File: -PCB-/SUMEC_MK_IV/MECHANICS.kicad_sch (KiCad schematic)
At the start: 20 parts, among them J13 Conn_01x06_Socket, J14 Conn_01x06_Socket, SW2 SW_Push, SW3 SW_Push, SW4 SW_Push, SW5 SW_Push, SW6 SW_Push

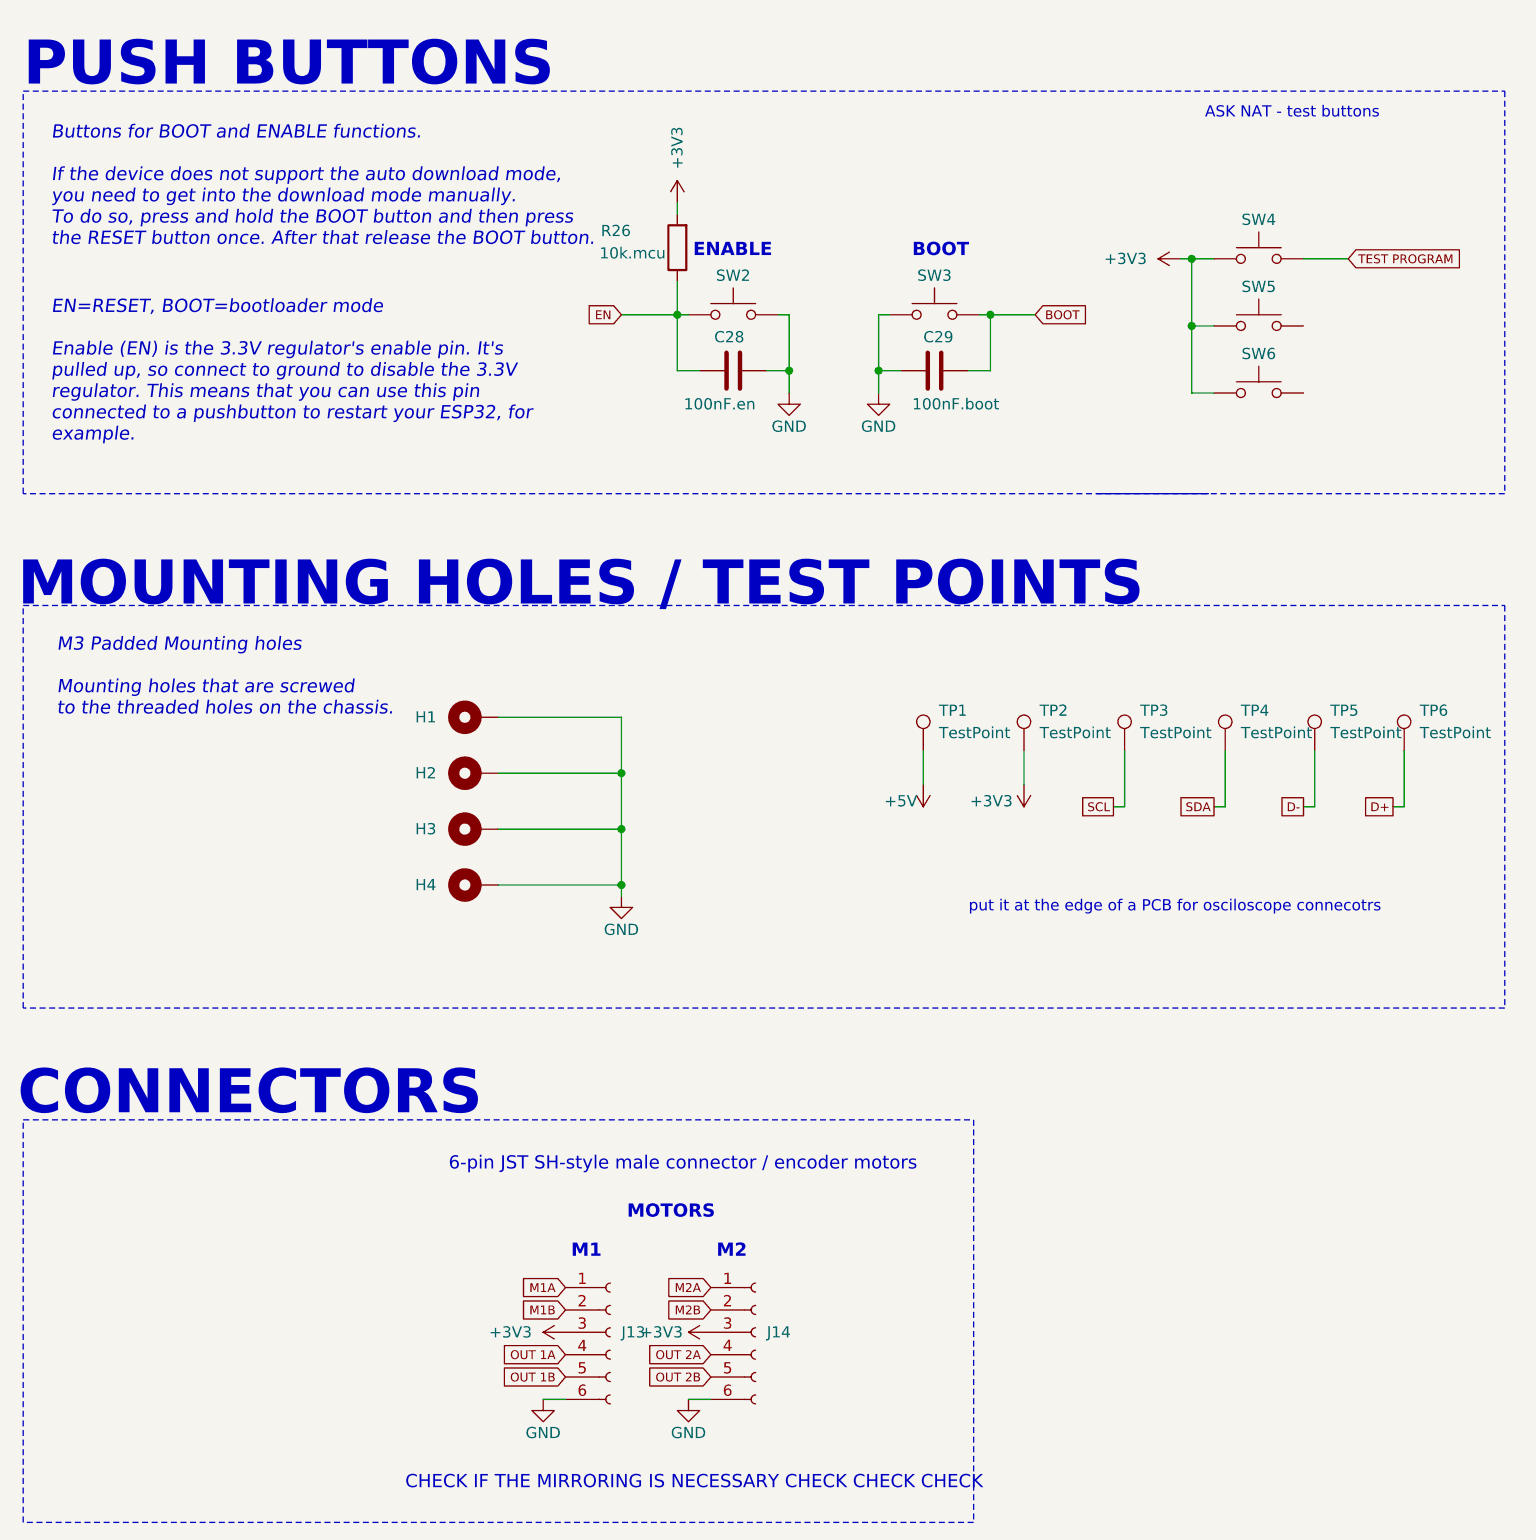
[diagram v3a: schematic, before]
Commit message: 3v3 buck redesign
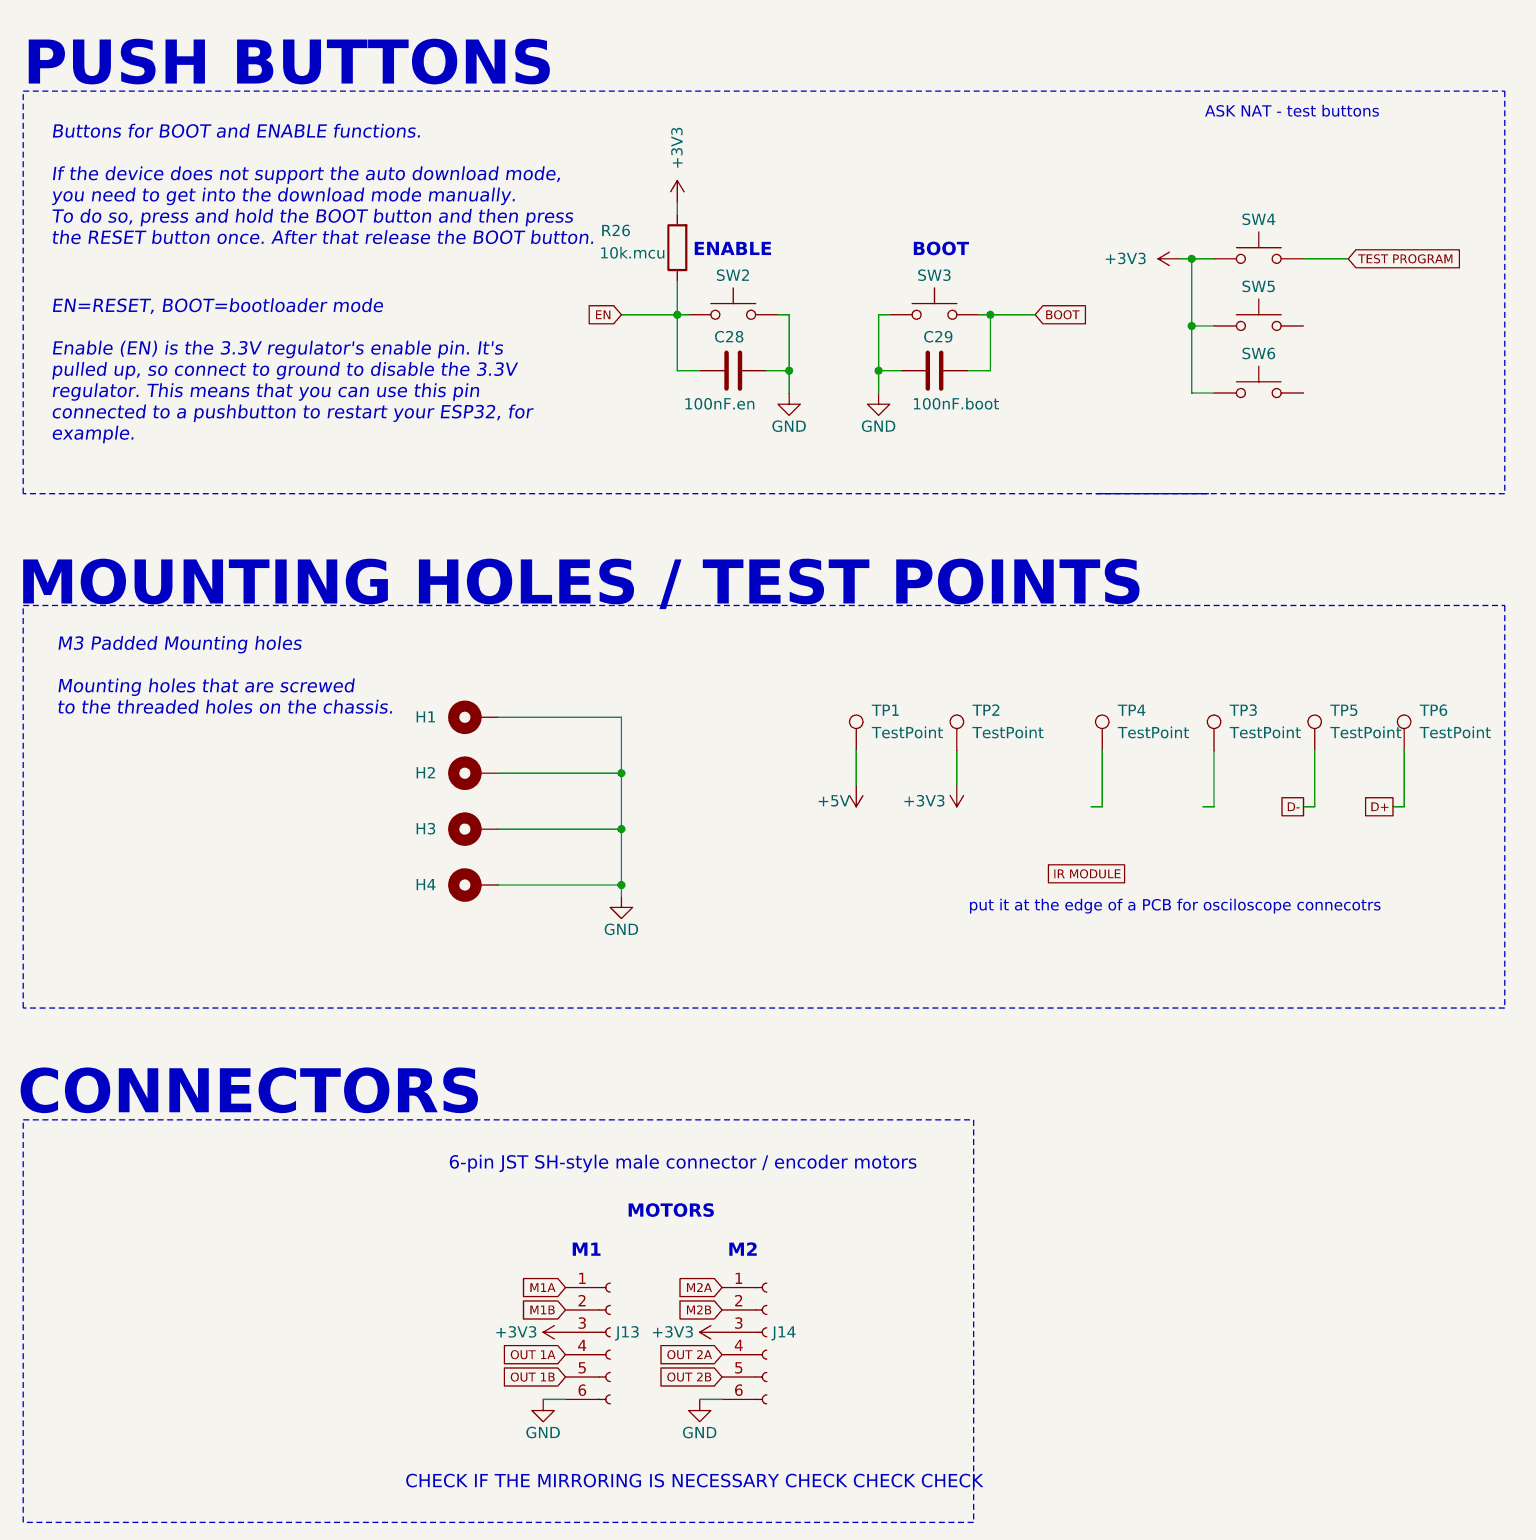
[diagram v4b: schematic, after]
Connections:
- net SCL: no longer names the net of TP3.1
- net SDA: no longer names the net of TP4.1
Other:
- moved on the sheet: J14, TP1, TP2, TP3, TP4

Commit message: Update update update
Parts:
- removed SW6: SW_Push, Button_Switch_SMD:SW_SPST_B3U-1000P, symbol Switch:SW_Push
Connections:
- net TEST PROGRAM 2: now reaches SW5.2
- net TEST PROGRAM renamed TEST PROGRAM 1
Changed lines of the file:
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@@
 		(color 0 0 0 0)
 	)
-	(junction
-		(at 167.64 52.07)
-		(diameter 0)
-		(color 0 0 0 0)
-	)
 	(wire
 		(pts
@@
 	(wire
 		(pts
-			(xy 170.18 59.69) (xy 167.64 59.69)
-		)
-		(stroke
-			(width 0)
-			(type default)
-		)
-	)
-	(wire
-		(pts
 			(xy 88.9 96.52) (xy 102.87 96.52)
 		)
@@
 		)
 	)
+	(wire
+		(pts
+			(xy 185.42 52.07) (xy 180.34 52.07)
+		)
+		(stroke
+			(width 0)
+			(type default)
+		)
+	)
 	(polyline
 		(pts
@@
 	(wire
 		(pts
-			(xy 167.64 59.69) (xy 167.64 52.07)
-		)
-		(stroke
-			(width 0)
-			(type default)
-		)
-	)
-	(wire
-		(pts
 			(xy 181.61 106.68) (xy 181.61 100.33)
 		)
@@
 		)
 	)
-	(global_label "TEST PROGRAM"
+	(global_label "TEST PROGRAM 2"
+		(shape input)
+		(at 185.42 52.07 0)
+		(fields_autoplaced yes)
+		(effects
+			(font
+				(face "Bahnschrift")
+				(size 1 1)
+				(color 0 0 0 1)
+			)
+			(justify left)
+		)
+		(property "Intersheetrefs" "${INTERSHEET_REFS}"
+			(at 198.5266 52.07 0)
+			(effects
+				(font
+					(size 1.27 1.27)
+				)
+				(justify left)
+				(hide yes)
+			)
+		)
+	)
+	(global_label "TEST PROGRAM 1"
 		(shape input)
 		(at 185.42 44.45 0)
@@
 		)
 		(property "Intersheetrefs" "${INTERSHEET_REFS}"
-			(at 198.8984 44.45 0)
+			(at 198.2687 44.45 0)
 			(effects
 				(font
@@
 	(global_label "IR MODULE"
 		(shape passive)
-		(at 160.02 114.3 180)
+		(at 139.7 118.11 180)
 		(fields_autoplaced yes)
 		(effects
@@
 		)
 		(property "Intersheetrefs" "${INTERSHEET_REFS}"
-			(at 151.6338 114.3 0)
+			(at 131.3138 118.11 0)
 			(effects
 				(font
@@
 	)
 	(symbol
-		(lib_id "Switch:SW_Push")
-		(at 175.26 59.69 0)
-		(unit 1)
-		(exclude_from_sim no)
-		(in_bom yes)
-		(on_board yes)
-		(dnp no)
-		(property "Reference" "SW6"
-			(at 175.26 55.245 0)
-			(effects
-				(font
-					(face "Bahnschrift")
-					(size 1.27 1.27)
-				)
-			)
-		)
-		(property "Value" "SW_Push"
-			(at 175.26 55.88 0)
-			(effects
-				(font
-					(face "Bahnschrift")
-					(size 1.27 1.27)
-				)
-				(hide yes)
-			)
-		)
-		(property "Footprint" "Button_Switch_SMD:SW_SPST_B3U-1000P"
-			(at 175.26 54.61 0)
-			(effects
-				(font
-					(face "Bahnschrift")
-					(size 1.27 1.27)
-				)
-				(hide yes)
-			)
-		)
-		(property "Datasheet" "~"
-			(at 175.26 54.61 0)
-			(effects
-				(font
-					(face "Bahnschrift")
-					(size 1.27 1.27)
-				)
-				(hide yes)
-			)
-		)
-		(property "Description" ""
-			(at 175.26 59.69 0)
-			(effects
-				(font
-					(size 1.27 1.27)
-				)
-				(hide yes)
-			)
-		)
-		(pin "1"
-		)
-		(pin "2"
-		)
-		(instances
-			(project "SUMEC_MK_IV"
-				(path "/900bd7ac-cdf9-4a2f-8b1f-2c21e3760046/a907f0f2-2950-481d-8037-7b9f13f2e9c5"
-					(reference "SW6")
-					(unit 1)
-				)
-			)
-		)
-	)
-	(symbol
 		(lib_id "Connector:TestPoint")
 		(at 140.97 100.33 0)
@@
 		)
 		(instances
-			(project ""
+			(project "SUMEC_MK_IV"
 				(path "/900bd7ac-cdf9-4a2f-8b1f-2c21e3760046/a907f0f2-2950-481d-8037-7b9f13f2e9c5"
 					(reference "J13")

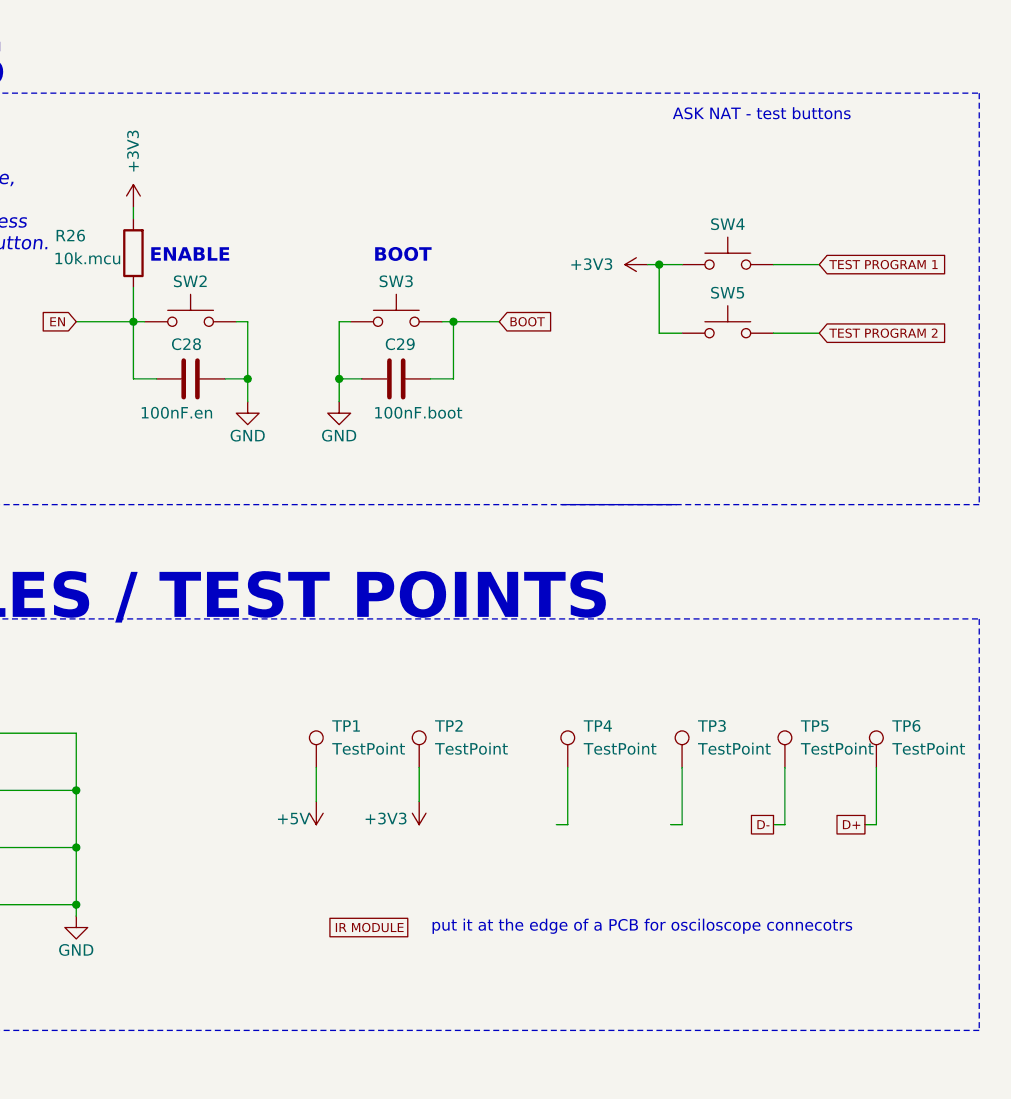
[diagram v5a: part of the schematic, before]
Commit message: Footprints added
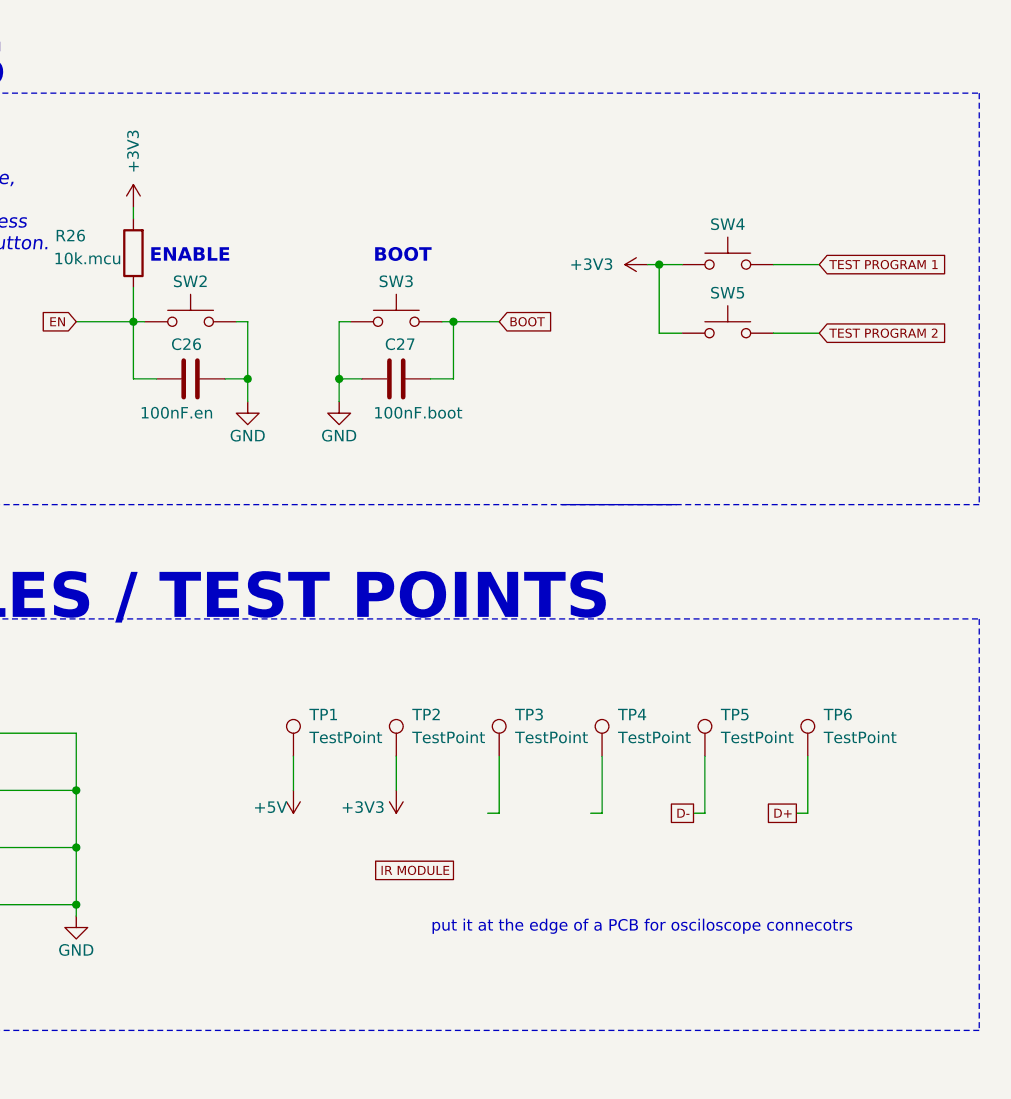
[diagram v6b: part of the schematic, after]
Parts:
- J13, J14: footprint (none) -> Connector_JST:JST_SH_SM06B-SRSS-TB_1x06-1MP_P1.00mm_Horizontal
- SW2, SW3, SW4, SW5: footprint Button_Switch_SMD:SW_SPST_B3U-1000P -> Button_Switch_SMD:SW_SPST_EVQPE1
- TP1: footprint TestPoint:TestPoint_Pad_D1.5mm -> TestPoint:TestPoint_Pad_D1.0mm
- TP3: renamed from TP4; footprint TestPoint:TestPoint_Pad_D1.5mm -> TestPoint:TestPoint_Pad_1.0x1.0mm
- renumbered C28 to C26, C29 to C27, TP3 to TP4
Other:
- note removed: "ASK NAT - test buttons"
- moved on the sheet: TP1, TP2, TP3, TP4, TP5, TP6

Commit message: MK_IV layout update
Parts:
- removed TP6: TestPoint, TestPoint:TestPoint_Pad_D1.5mm, symbol Connector:TestPoint
- TP1: footprint TestPoint:TestPoint_Pad_D1.0mm -> TestPoint:TestPoint_Pad_1.0x1.0mm
- TP2: footprint TestPoint:TestPoint_Loop_D1.80mm_Drill1.0mm_Beaded -> TestPoint:TestPoint_Pad_1.0x1.0mm
- TP4, TP5: footprint TestPoint:TestPoint_Pad_D1.5mm -> TestPoint:TestPoint_Pad_1.0x1.0mm
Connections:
- net D- is gone; now on net OUT 1B: TP5.1
- net IR MODULE: now also TP3.1
- net OUT 1A: now also TP4.1

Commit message: PCB routing
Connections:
- net +3V3: now also J13.4 (Pin_4), J14.4 (Pin_4); no longer J13.3 (Pin_3), J14.3 (Pin_3)
- net GND: now also J13.1 (Pin_1), J14.1 (Pin_1); no longer J13.6 (Pin_6), J14.6 (Pin_6)
- net IR MODULE: now also TP5.1; no longer TP3.1
- net M1A: now also J13.6 (Pin_6); no longer J13.1 (Pin_1)
- net M1B: now also J13.5 (Pin_5); no longer J13.2 (Pin_2)
- net M2A: now also J14.6 (Pin_6); no longer J14.1 (Pin_1)
- net M2B: now also J14.5 (Pin_5); no longer J14.2 (Pin_2)
- net OUT 1A: now also J13.3 (Pin_3), TP3.1; no longer J13.4 (Pin_4), TP4.1
- net OUT 1B: now also J13.2 (Pin_2), TP4.1; no longer J13.5 (Pin_5), TP5.1
- net OUT 2A: now also J14.3 (Pin_3); no longer J14.4 (Pin_4)
- net OUT 2B: now also J14.2 (Pin_2); no longer J14.5 (Pin_5)
